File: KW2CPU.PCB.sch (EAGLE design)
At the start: 58 parts, among them J1 DF12_M, J2 MOLEX55560-0207, J3 MMCX_VERT, U1 MKW21D, U2 AT45DB161D8S1, U3 RF6555, U5 F-ANTENNA, X1 32KHZ, X2 32MHZ

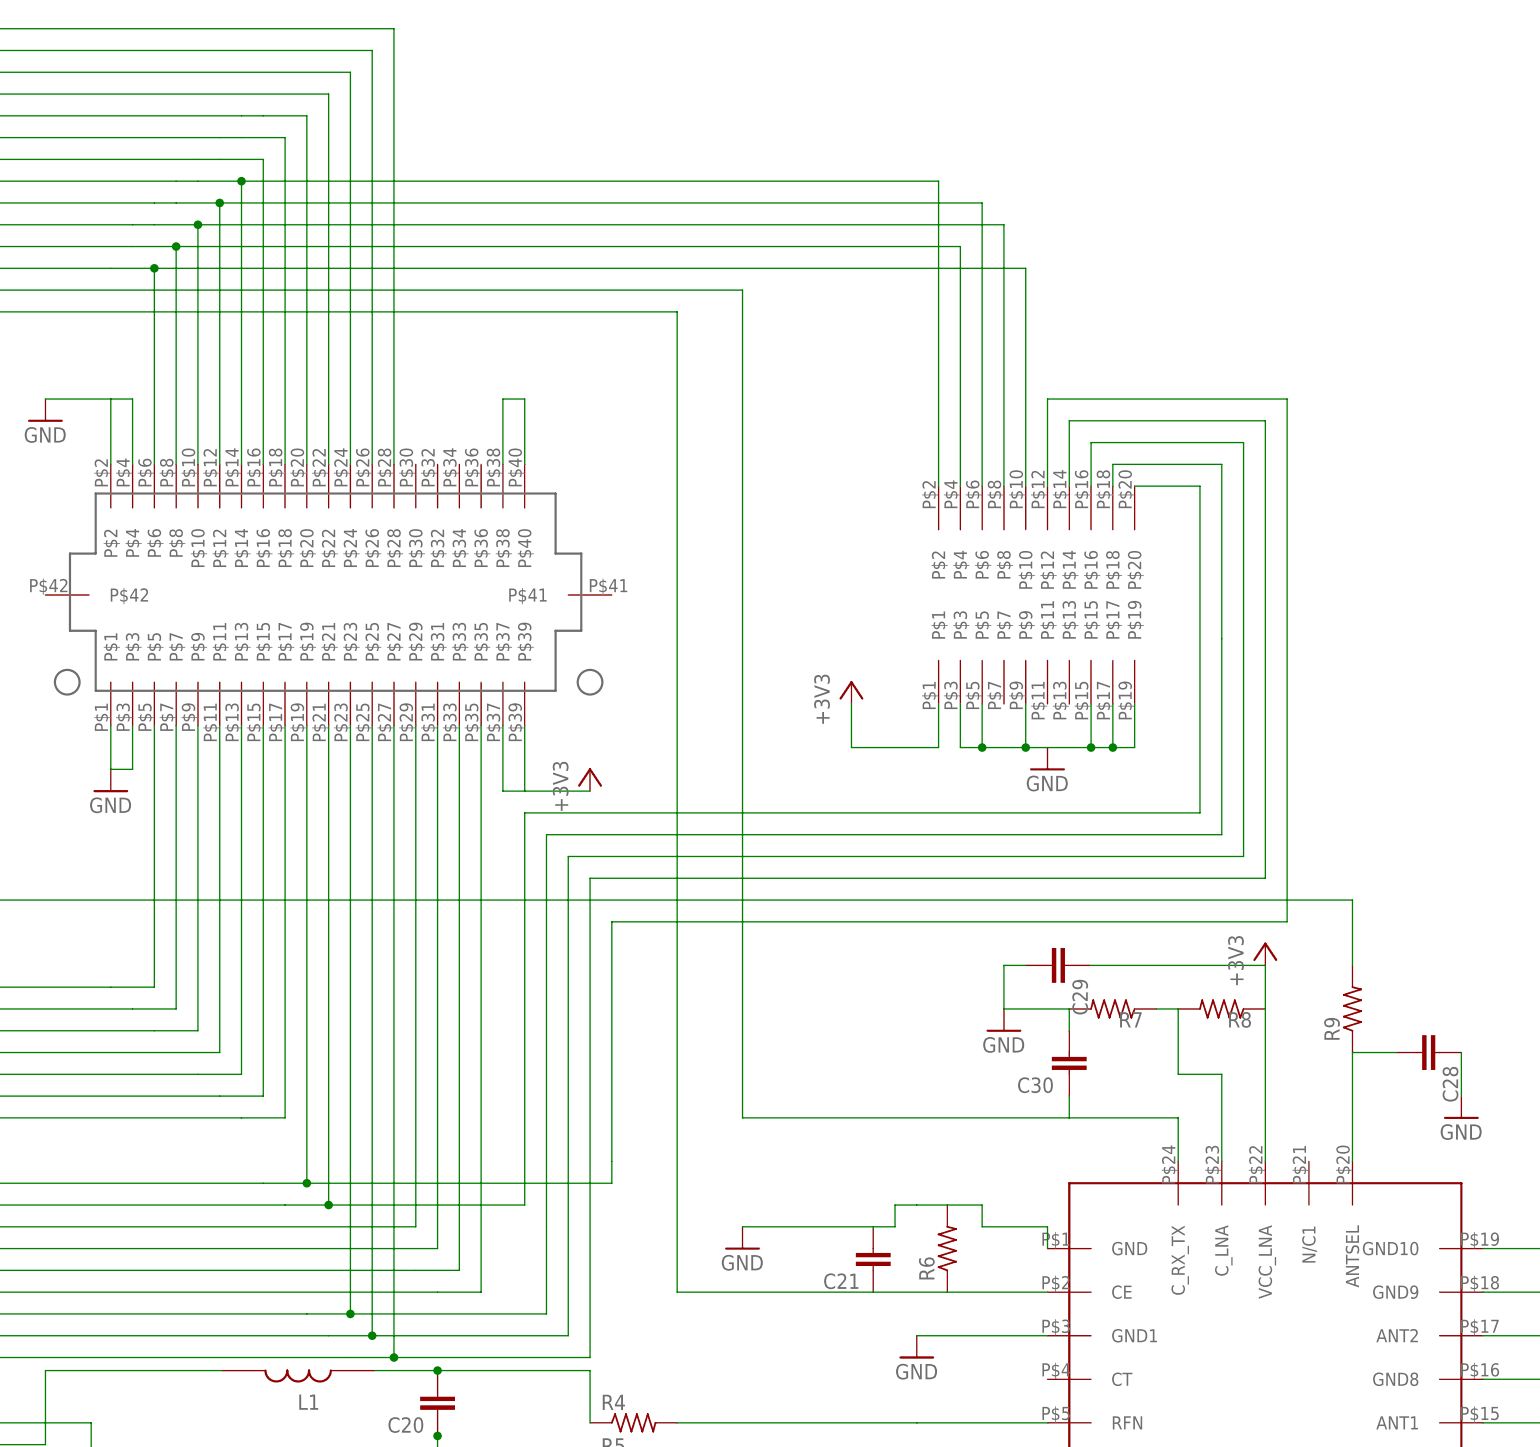
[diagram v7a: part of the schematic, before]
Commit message: Added test points
JTAG and front-end control test points
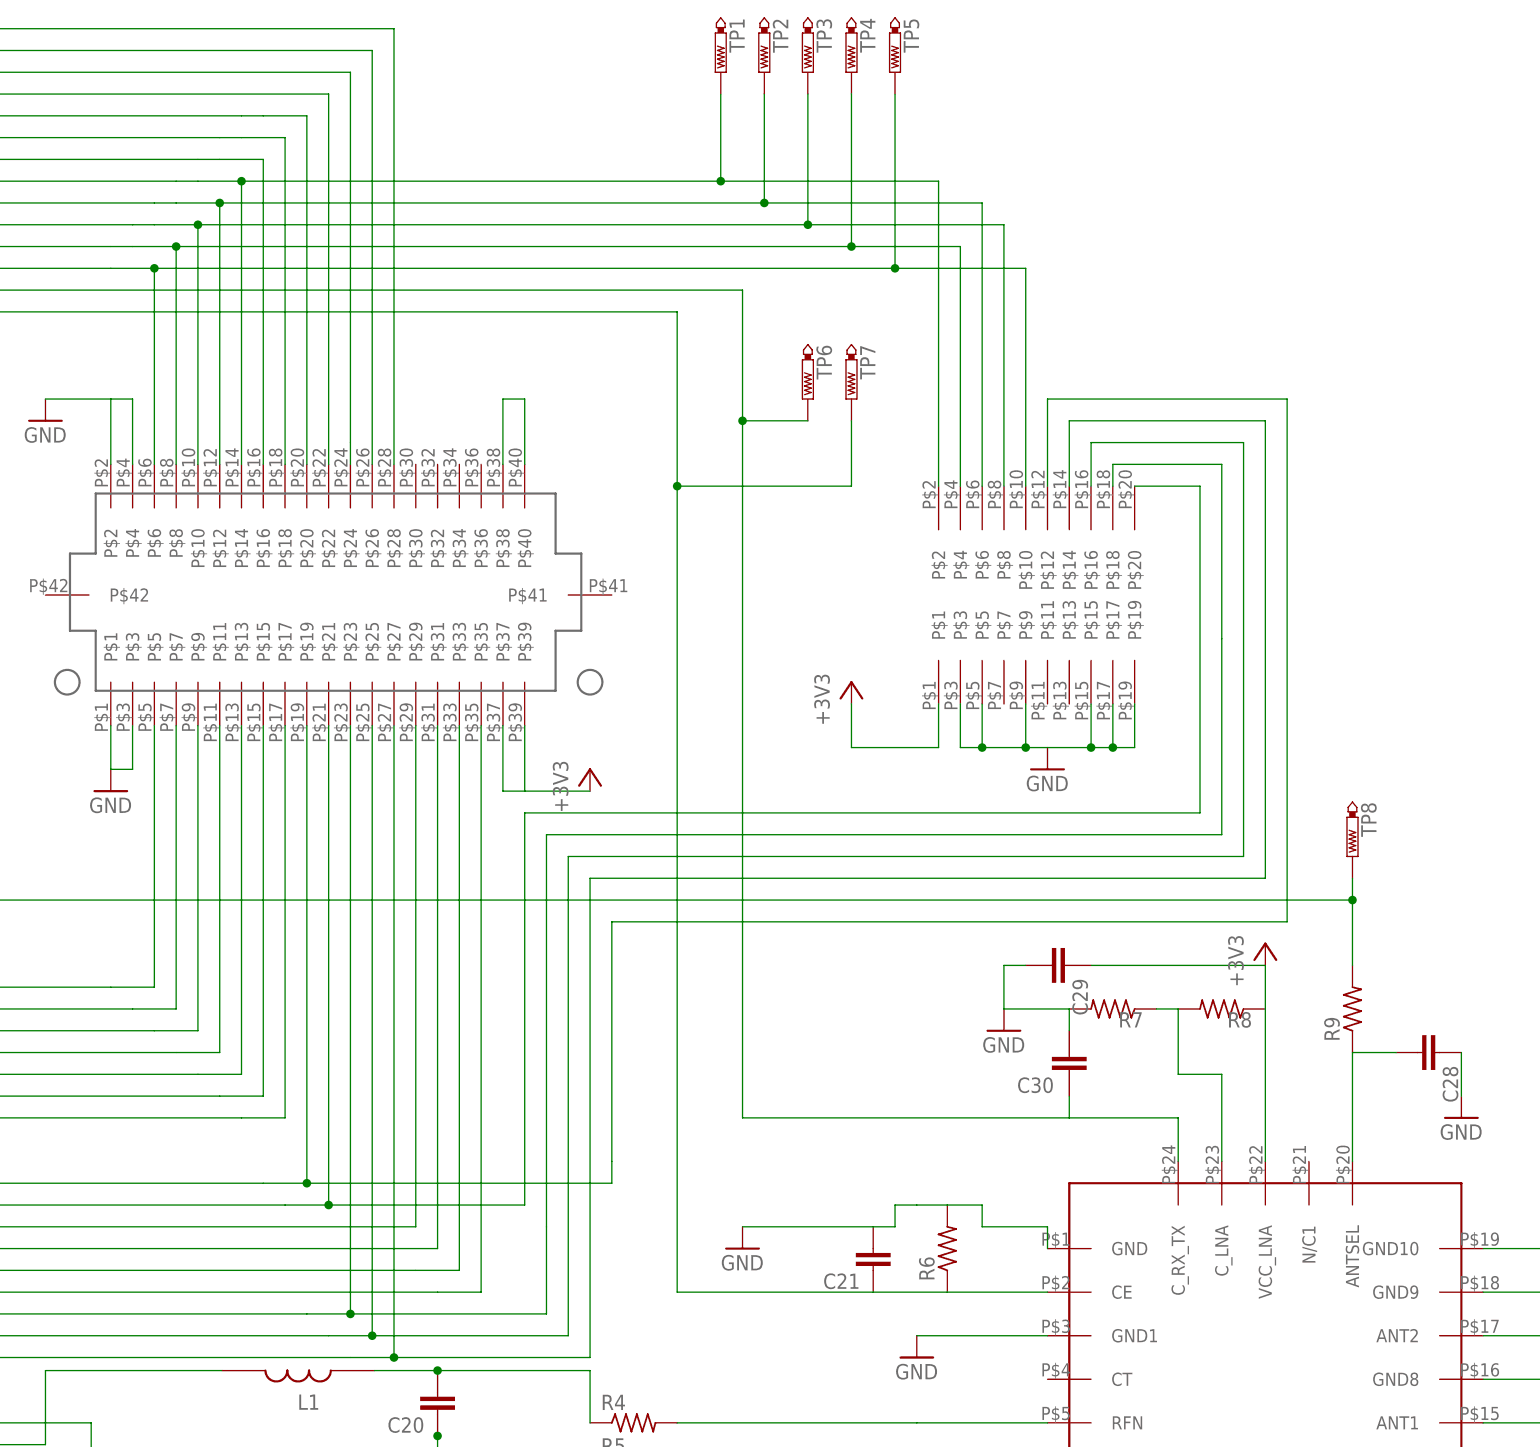
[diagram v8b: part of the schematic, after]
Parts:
- added TP1, TP2, TP3, TP4, TP5, TP6, TP7, TP8: PTR1TP15R, testpad:PTR1TP15R
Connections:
- net !RESET: now also TP5.TP
- net ANT_A: now also TP8.TP
- net PTA0/JTAG_TCLK/SWD_CLK/EZP_CLK/!UART0_CTS/!UART0_COL/FTM0_CH5: now also TP4.TP
- net PTA1/JTAG_TDI/EZP_DI/UART0/RX/FTM0_CH6: now also TP3.TP
- net PTA2/JTAG_TDO/TRACE?SWO/EZP_DO/UART0_TX/FTM0_CH7: now also TP2.TP
- net PTA3/JTAG_TMS/SWD_DIO/UART0_RTS/FTM0_CH0: now also TP1.TP
- net RX_SWITCH: now also TP7.TP
- net TX_SWITCH: now also TP6.TP
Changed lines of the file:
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@@
 <attribute name="MFGP" value="ERJ-2GEJ513X"/>
 </part>
+<part name="TP1" library="testpad" deviceset="PTR1" device="TP15R"/>
+<part name="TP2" library="testpad" deviceset="PTR1" device="TP15R"/>
+<part name="TP3" library="testpad" deviceset="PTR1" device="TP15R"/>
+<part name="TP4" library="testpad" deviceset="PTR1" device="TP15R"/>
+<part name="TP5" library="testpad" deviceset="PTR1" device="TP15R"/>
+<part name="TP6" library="testpad" deviceset="PTR1" device="TP15R"/>
+<part name="TP7" library="testpad" deviceset="PTR1" device="TP15R"/>
+<part name="TP8" library="testpad" deviceset="PTR1" device="TP15R"/>
 </parts>
 <sheets>
@@
 <attribute name="VALUE" x="333.756" y="40.259" size="1.778" layer="96" rot="R180"/>
 </instance>
+<instance part="TP1" gate="G$1" x="276.86" y="144.78" rot="R180"/>
+<instance part="TP2" gate="G$1" x="281.94" y="144.78" rot="R180"/>
+<instance part="TP3" gate="G$1" x="287.02" y="144.78" rot="R180"/>
+<instance part="TP4" gate="G$1" x="292.1" y="144.78" rot="R180"/>
+<instance part="TP5" gate="G$1" x="297.18" y="144.78" rot="R180"/>
+<instance part="TP6" gate="G$1" x="287.02" y="106.68" rot="R180"/>
+<instance part="TP7" gate="G$1" x="292.1" y="106.68" rot="R180"/>
+<instance part="TP8" gate="G$1" x="350.52" y="53.34" rot="R180"/>
 </instances>
 <busses>
@@
 <pinref part="R9" gate="G$1" pin="2"/>
 <wire x1="350.52" y1="40.64" x2="350.52" y2="48.26" width="0.1524" layer="91"/>
+<pinref part="TP8" gate="G$1" pin="TP"/>
+<wire x1="350.52" y1="50.8" x2="350.52" y2="48.26" width="0.1524" layer="91"/>
+<junction x="350.52" y="48.26"/>
 </segment>
 </net>
@@
 <wire x1="330.2" y1="22.86" x2="317.5" y2="22.86" width="0.1524" layer="91"/>
 <wire x1="317.5" y1="22.86" x2="279.4" y2="22.86" width="0.1524" layer="91"/>
-<wire x1="279.4" y1="22.86" x2="279.4" y2="119.38" width="0.1524" layer="91"/>
+<wire x1="279.4" y1="22.86" x2="279.4" y2="104.14" width="0.1524" layer="91"/>
+<wire x1="279.4" y1="104.14" x2="279.4" y2="119.38" width="0.1524" layer="91"/>
 <wire x1="279.4" y1="119.38" x2="-157.48" y2="119.38" width="0.1524" layer="91"/>
 <wire x1="-157.48" y1="119.38" x2="-157.48" y2="-5.08" width="0.1524" layer="91"/>
@@
 <pinref part="C30" gate="G$1" pin="2"/>
 <wire x1="317.5" y1="25.4" x2="317.5" y2="22.86" width="0.1524" layer="91"/>
+<pinref part="TP6" gate="G$1" pin="TP"/>
+<wire x1="287.02" y1="104.14" x2="279.4" y2="104.14" width="0.1524" layer="91"/>
+<junction x="279.4" y="104.14"/>
 </segment>
 </net>
@@
 <wire x1="314.96" y1="2.54" x2="303.276" y2="2.54" width="0.1524" layer="91"/>
 <wire x1="294.64" y1="2.54" x2="271.78" y2="2.54" width="0.1524" layer="91"/>
-<wire x1="271.78" y1="2.54" x2="271.78" y2="116.84" width="0.1524" layer="91"/>
+<wire x1="271.78" y1="2.54" x2="271.78" y2="96.52" width="0.1524" layer="91"/>
+<wire x1="271.78" y1="96.52" x2="271.78" y2="116.84" width="0.1524" layer="91"/>
 <wire x1="271.78" y1="116.84" x2="-154.94" y2="116.84" width="0.1524" layer="91"/>
 <wire x1="-154.94" y1="116.84" x2="-154.94" y2="-2.54" width="0.1524" layer="91"/>
@@
 <pinref part="U1" gate="G$1" pin="RX_SWITCH"/>
 <wire x1="-129.54" y1="0" x2="-66.04" y2="0" width="0.1524" layer="91"/>
+<pinref part="TP7" gate="G$1" pin="TP"/>
+<wire x1="292.1" y1="104.14" x2="292.1" y2="96.52" width="0.1524" layer="91"/>
+<wire x1="292.1" y1="96.52" x2="271.78" y2="96.52" width="0.1524" layer="91"/>
+<junction x="271.78" y="96.52"/>
 </segment>
 </net>
@@
 <wire x1="208.28" y1="124.46" x2="213.36" y2="124.46" width="0.1524" layer="91"/>
 <wire x1="213.36" y1="124.46" x2="213.36" y2="99.06" width="0.1524" layer="91"/>
-<wire x1="213.36" y1="124.46" x2="304.8" y2="124.46" width="0.1524" layer="91"/>
+<wire x1="213.36" y1="124.46" x2="292.1" y2="124.46" width="0.1524" layer="91"/>
+<wire x1="292.1" y1="124.46" x2="304.8" y2="124.46" width="0.1524" layer="91"/>
 <wire x1="304.8" y1="124.46" x2="304.8" y2="96.52" width="0.1524" layer="91"/>
 <junction x="213.36" y="124.46"/>
 <pinref part="J2" gate="G$1" pin="P$4"/>
+<pinref part="TP4" gate="G$1" pin="TP"/>
+<wire x1="292.1" y1="142.24" x2="292.1" y2="124.46" width="0.1524" layer="91"/>
+<junction x="292.1" y="124.46"/>
 </segment>
 </net>
@@
 <wire x1="210.82" y1="127" x2="215.9" y2="127" width="0.1524" layer="91"/>
 <wire x1="215.9" y1="127" x2="215.9" y2="99.06" width="0.1524" layer="91"/>
-<wire x1="215.9" y1="127" x2="309.88" y2="127" width="0.1524" layer="91"/>
+<wire x1="215.9" y1="127" x2="287.02" y2="127" width="0.1524" layer="91"/>
 <junction x="215.9" y="127"/>
 <pinref part="J2" gate="G$1" pin="P$8"/>
+<wire x1="287.02" y1="127" x2="309.88" y2="127" width="0.1524" layer="91"/>
 <wire x1="309.88" y1="127" x2="309.88" y2="96.52" width="0.1524" layer="91"/>
+<pinref part="TP3" gate="G$1" pin="TP"/>
+<wire x1="287.02" y1="142.24" x2="287.02" y2="127" width="0.1524" layer="91"/>
+<junction x="287.02" y="127"/>
 </segment>
 </net>
@@
 <wire x1="213.36" y1="129.54" x2="218.44" y2="129.54" width="0.1524" layer="91"/>
 <wire x1="218.44" y1="129.54" x2="218.44" y2="99.06" width="0.1524" layer="91"/>
-<wire x1="218.44" y1="129.54" x2="307.34" y2="129.54" width="0.1524" layer="91"/>
+<wire x1="218.44" y1="129.54" x2="281.94" y2="129.54" width="0.1524" layer="91"/>
+<wire x1="281.94" y1="129.54" x2="307.34" y2="129.54" width="0.1524" layer="91"/>
 <wire x1="307.34" y1="129.54" x2="307.34" y2="96.52" width="0.1524" layer="91"/>
 <junction x="218.44" y="129.54"/>
 <pinref part="J2" gate="G$1" pin="P$6"/>
+<pinref part="TP2" gate="G$1" pin="TP"/>
+<wire x1="281.94" y1="142.24" x2="281.94" y2="129.54" width="0.1524" layer="91"/>
+<junction x="281.94" y="129.54"/>
 </segment>
 </net>
@@
 <wire x1="220.98" y1="132.08" x2="220.98" y2="99.06" width="0.1524" layer="91"/>
 <junction x="220.98" y="132.08"/>
-<wire x1="220.98" y1="132.08" x2="302.26" y2="132.08" width="0.1524" layer="91"/>
+<wire x1="220.98" y1="132.08" x2="276.86" y2="132.08" width="0.1524" layer="91"/>
+<wire x1="276.86" y1="132.08" x2="302.26" y2="132.08" width="0.1524" layer="91"/>
 <wire x1="302.26" y1="132.08" x2="302.26" y2="96.52" width="0.1524" layer="91"/>
 <pinref part="J2" gate="G$1" pin="P$2"/>
+<pinref part="TP1" gate="G$1" pin="TP"/>
+<wire x1="276.86" y1="142.24" x2="276.86" y2="132.08" width="0.1524" layer="91"/>
+<junction x="276.86" y="132.08"/>
 </segment>
 </net>
@@
 <wire x1="205.74" y1="121.92" x2="210.82" y2="121.92" width="0.1524" layer="91"/>
 <wire x1="210.82" y1="121.92" x2="210.82" y2="99.06" width="0.1524" layer="91"/>
-<wire x1="210.82" y1="121.92" x2="312.42" y2="121.92" width="0.1524" layer="91"/>
+<wire x1="210.82" y1="121.92" x2="297.18" y2="121.92" width="0.1524" layer="91"/>
+<wire x1="297.18" y1="121.92" x2="312.42" y2="121.92" width="0.1524" layer="91"/>
 <wire x1="312.42" y1="121.92" x2="312.42" y2="96.52" width="0.1524" layer="91"/>
 <junction x="210.82" y="121.92"/>
 <pinref part="J2" gate="G$1" pin="P$10"/>
-</segment>
-</net>
+<pinref part="TP5" gate="G$1" pin="TP"/>
+<wire x1="297.18" y1="142.24" x2="297.18" y2="121.92" width="0.1524" layer="91"/>
+<junction x="297.18" y="121.92"/>
+</segment>
+</net>
